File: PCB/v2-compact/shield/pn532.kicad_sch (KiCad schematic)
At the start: 0 parts

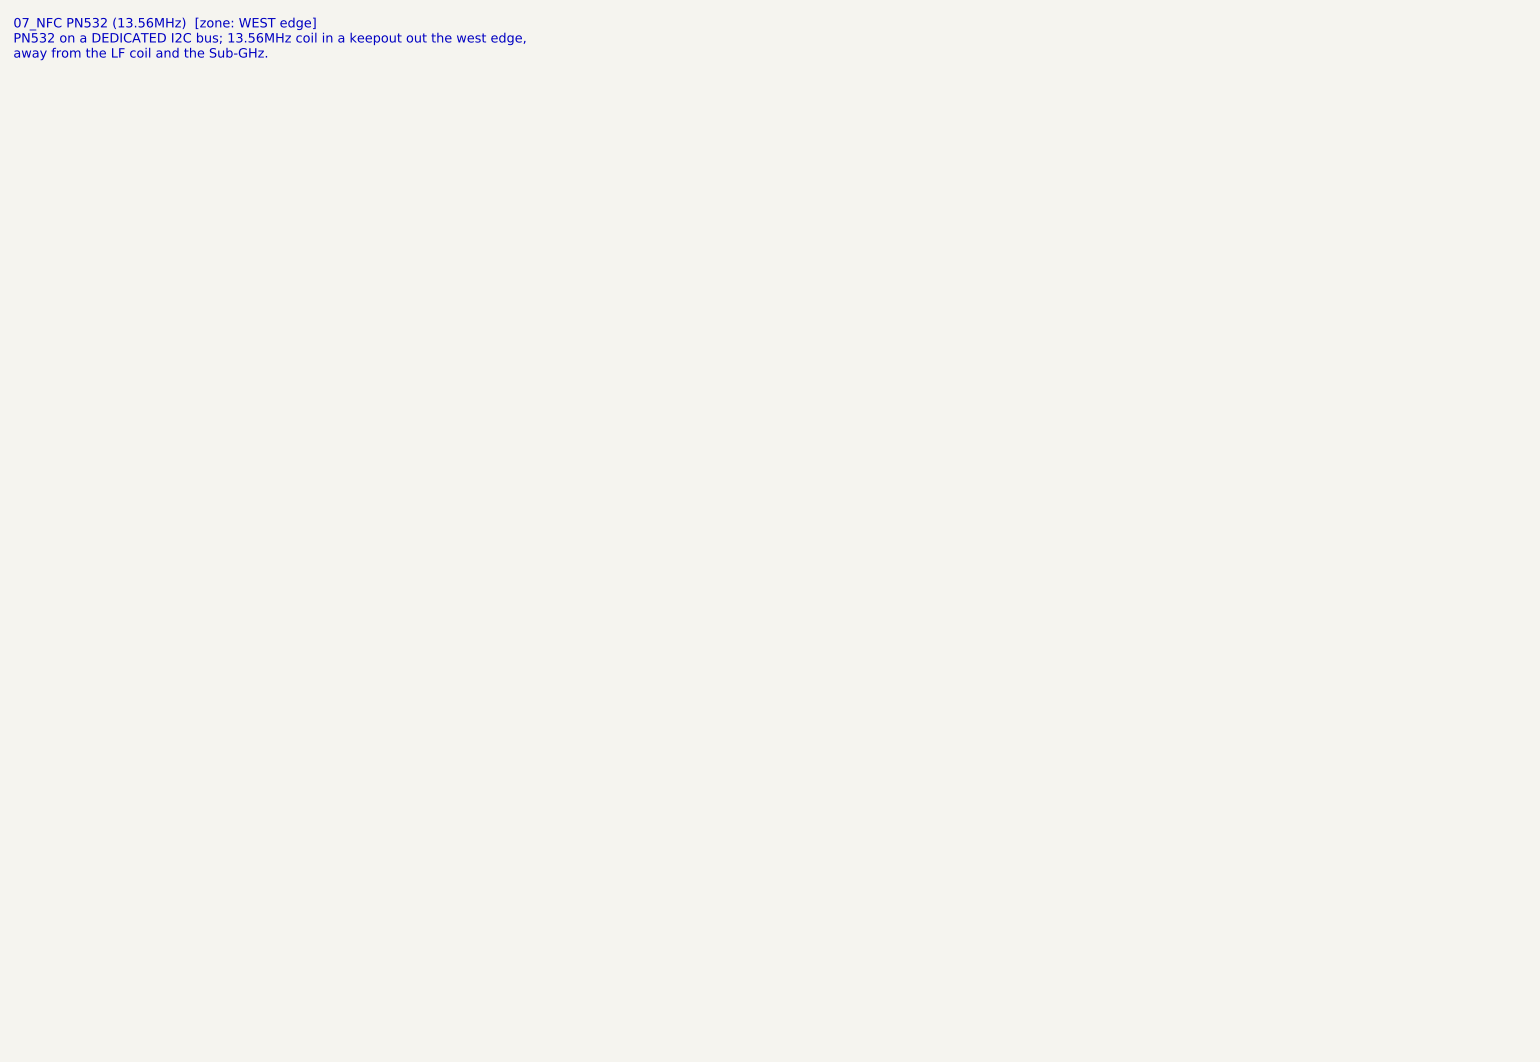
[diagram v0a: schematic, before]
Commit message: Schematics: capture PN532, GPS, IR, and both power sheets
- 07_NFC_PN532: I2C mode (I0/I1 set), 27.12MHz crystal, VMID cap, internal
  DVDD/SVDD regulator outputs correctly decoupled (not tied to 3V3), pull-ups;
  antenna pins flagged for the RF matching pass.
- 10_GPS: NEO-M9N UART to the C5, power + decoupling; bias-tee/antenna flagged.
- 11_IR: TSOP receiver + IR-LED transmitter (NPN driver).
- 02_Power (shield): local AP7361C LDO for the C5 rail + bulk caps + PWR_FLAGs.
- 01_Power_USB (main): USB-C, CC resistors, USBLC6 ESD, AP7361C 3V3 LDO.

All netlist-verified. Remaining ERC items are expected WIP (no-connects on unused
IC pins + power flags), to be cleaned once the MCU sheets tie in the shared nets.
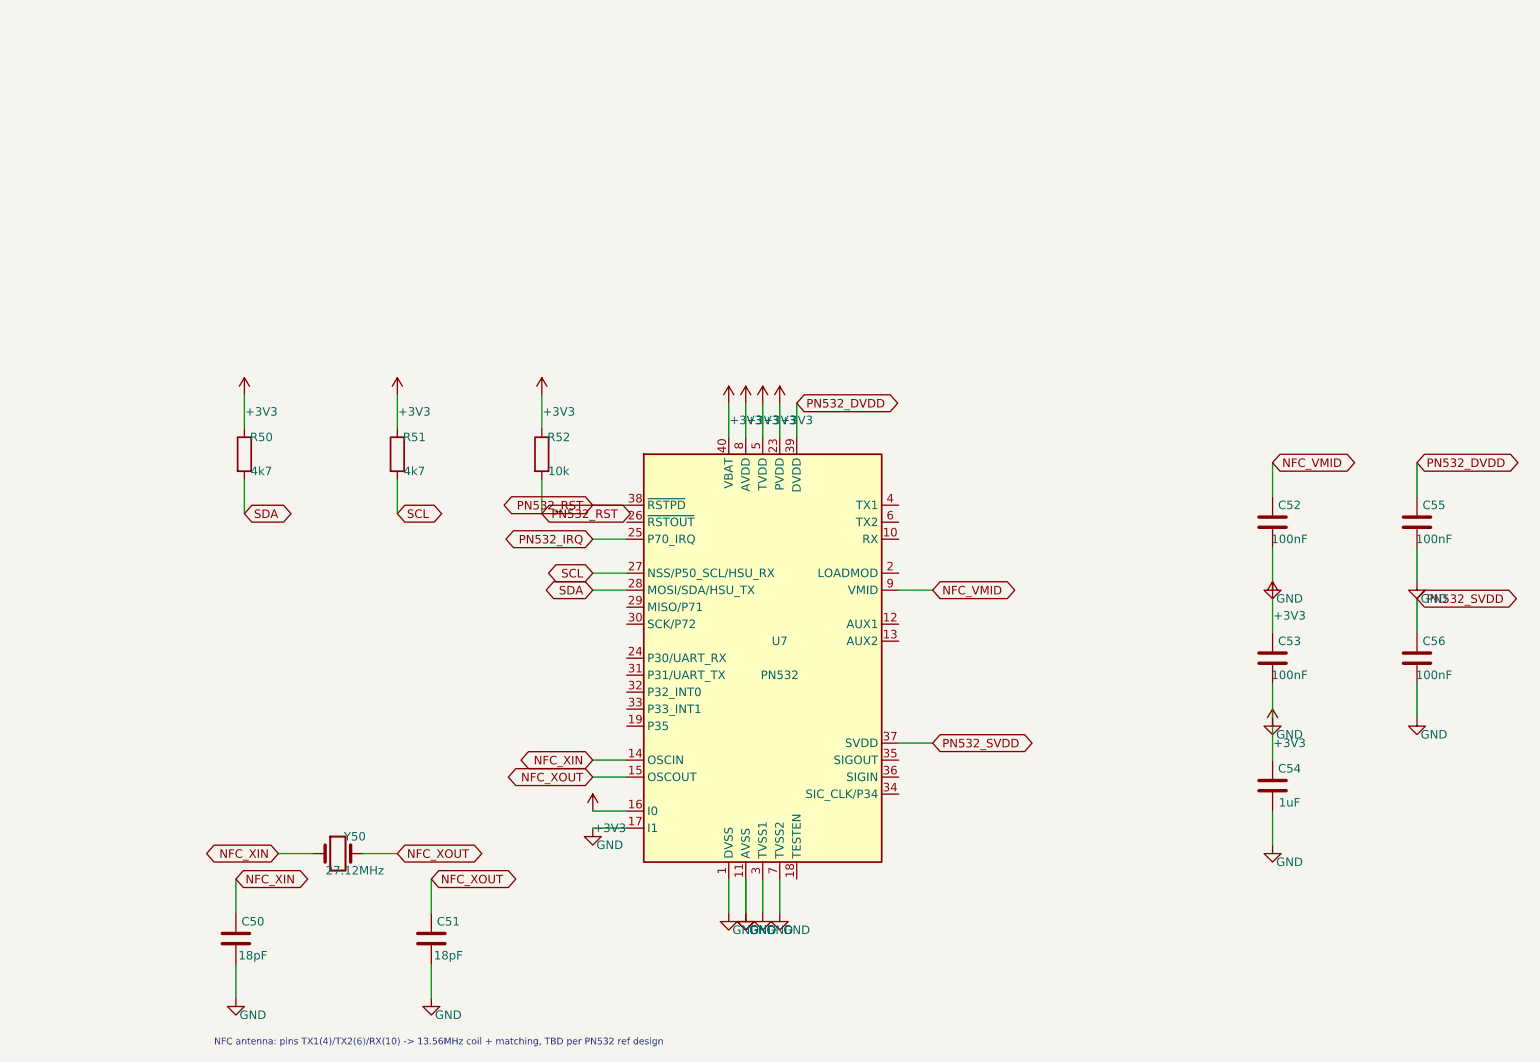
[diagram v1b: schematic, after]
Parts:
- added C50, C51: 18pF, Capacitor_SMD:C_0402_1005Metric, symbol Device:C
- added C52, C53, C55, C56: 100nF, Capacitor_SMD:C_0402_1005Metric, symbol Device:C
- added C54: 1uF, Capacitor_SMD:C_0402_1005Metric, symbol Device:C
- added R50, R51: 4k7, Resistor_SMD:R_0402_1005Metric, symbol Device:R
- added R52: 10k, Resistor_SMD:R_0402_1005Metric, symbol Device:R
- added U7: PN532, Package_DFN_QFN:HVQFN-40-1EP_6x6mm_P0.5mm_EP4.1x4.1mm, symbol RF_NFC:PN5321A3HN_C1xx
- added Y50: 27.12MHz, Crystal:Crystal_SMD_3225-4Pin_3.2x2.5mm, symbol Device:Crystal
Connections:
- new net +3V3: C53.1, C54.1, R50.1, R51.1, R52.1, U7.16 (I0), U7.23 (PVDD), U7.40 (VBAT), U7.5 (TVDD), U7.8 (AVDD)
- new net GND: C50.2, C51.2, C52.2, C53.2, C54.2, C55.2, C56.2, U7.1 (DVSS), U7.11 (AVSS), U7.17 (I1), U7.3 (TVSS1), U7.41 (AVSS), U7.7 (TVSS2)
- new net NFC_VMID: C52.1, U7.9 (VMID)
- new net NFC_XIN: C50.1, U7.14 (OSCIN), Y50.1
- new net NFC_XOUT: C51.1, U7.15 (OSCOUT), Y50.2
- new net PN532_DVDD: C55.1, U7.39 (DVDD)
- new net PN532_IRQ: U7.25 (P70_IRQ)
- new net PN532_RST: R52.2, U7.38 (~{RSTPD})
- new net PN532_SVDD: C56.1, U7.37 (SVDD)
- new net SCL: R51.2, U7.27 (NSS/P50_SCL/HSU_RX)
- new net SDA: R50.2, U7.28 (MOSI/SDA/HSU_TX)
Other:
- note added: "NFC antenna: pins TX1(4)/TX2(6)/RX(10) -> 13.56MHz coil + matching, TBD per PN532 ref design"
- note removed: "07_NFC PN532 (13.56MHz) [zone: WEST edge] PN532 on a DEDICATED I2C bus; 13.56MHz coil in a keepout out the west edge, away from the LF coil and the Sub-GHz."
